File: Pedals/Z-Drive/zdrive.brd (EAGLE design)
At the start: 55.9 x 54.6 mm, 30 parts, among them IC1 MC1458P, Q1 2N7000, Q2 2N7000

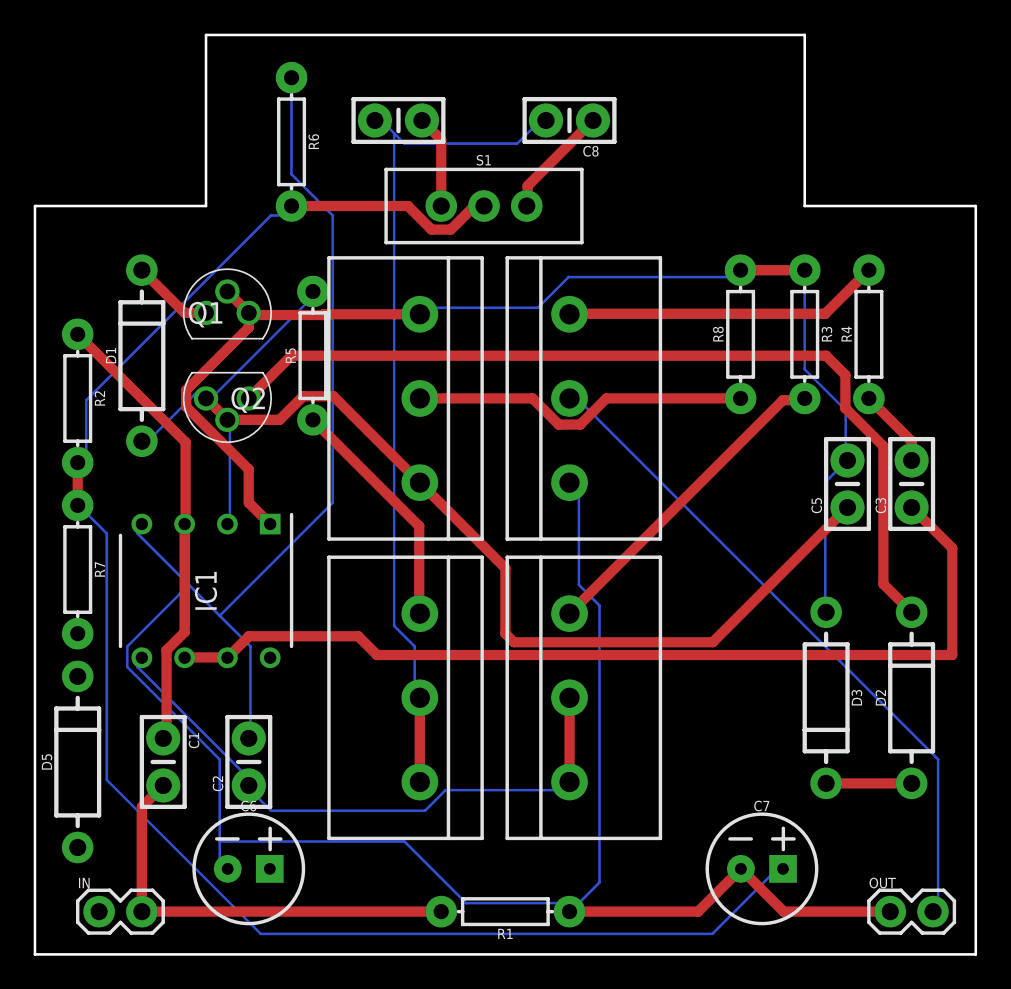
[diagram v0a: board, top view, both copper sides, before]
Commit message: Board routed V1
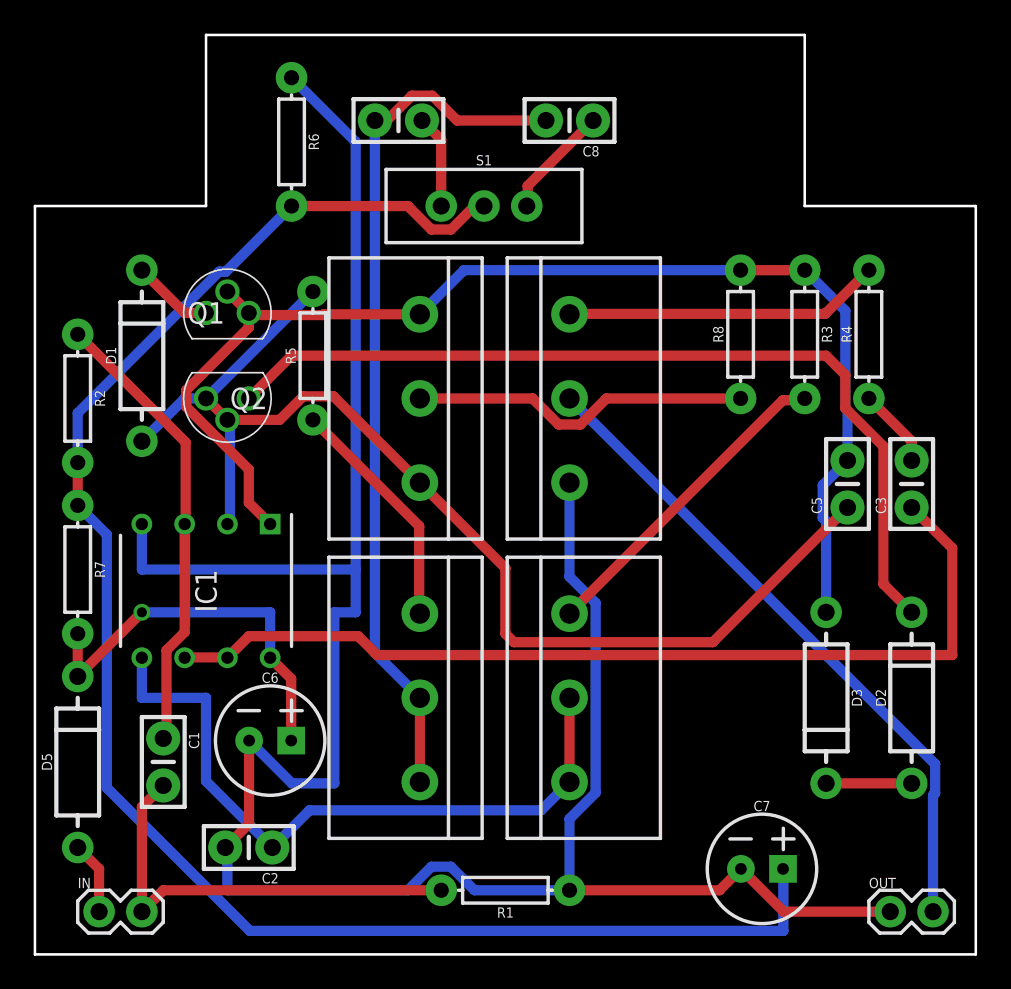
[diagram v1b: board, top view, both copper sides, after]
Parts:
- moved C6 7.73 mm to (14.0, 12.7)
- moved C2 5.08 mm to (12.7, 6.35), turned to 180 degrees
- moved R1 1.27 mm to (27.9, 3.81)
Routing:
- net V+: track 0.97 -> 23.7 mm, vias 0 -> 1
- net OP5: track 36.1 -> 41.0 mm
- net 9V: track 0.00 -> 4.34 mm
- net V2: track 99.1 -> 100.7 mm
- net N$7: track 50.6 -> 51.8 mm
- net OP2: track 71.8 -> 71.1 mm
- net IN: track 25.8 -> 26.3 mm

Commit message: Shift switch
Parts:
- moved S1 0.63 mm to (27.3, 44.5)
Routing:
- net V2: track 100.7 -> 101.4 mm
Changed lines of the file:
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@@
 <setting verticaltext="up"/>
 </settings>
-<grid distance="50" unitdist="mil" unit="mil" style="lines" multiple="1" display="yes" altdistance="5" altunitdist="mil" altunit="mil"/>
+<grid distance="25" unitdist="mil" unit="mil" style="lines" multiple="1" display="yes" altdistance="5" altunitdist="mil" altunit="mil"/>
 <layers>
 <layer number="1" name="Top" color="4" fill="1" visible="yes" active="yes"/>
@@
 </layers>
 <board>
-<fusionsync huburn="a.YnVzaW5lc3M6Z21haWwxNjcwNzYy" projecturn="a.YnVzaW5lc3M6Z21haWwxNjcwNzYyIzIwMjEwNDEyNDAyMDk1MzUx" f3durn="urn:adsk.wipprod:dm.lineage:s0TrARQBRNe1nJ0j_Cxp4Q" pcbguid="2e1078e5-0462-4d1c-b8a8-0c0597d6a6c0" lastpulledtime="" lastsyncedchangeguid="" latestrevisionid="c03cb7e0-1b01-40d5-a0a0-639d900d0ca0" lastsyncedrevisionid="c03cb7e0-1b01-40d5-a0a0-639d900d0ca0" lastboardhashguid="4b4d04b6-911f-26f5-6e83-cf409d0949b4" lastpushedtime="2021-04-13T14:10:19Z" linktopcb3d="true"/>
+<fusionsync huburn="a.YnVzaW5lc3M6Z21haWwxNjcwNzYy" projecturn="a.YnVzaW5lc3M6Z21haWwxNjcwNzYyIzIwMjEwNDEyNDAyMDk1MzUx" f3durn="urn:adsk.wipprod:dm.lineage:s0TrARQBRNe1nJ0j_Cxp4Q" pcbguid="" lastpulledtime="" lastsyncedchangeguid="" latestrevisionid="c03cb7e0-1b01-40d5-a0a0-639d900d0ca0" lastsyncedrevisionid="c03cb7e0-1b01-40d5-a0a0-639d900d0ca0" lastboardhashguid="4b4d04b6-911f-26f5-6e83-cf409d0949b4" lastpushedtime="2021-04-13T14:10:19Z" linktopcb3d="true"/>
 <plain>
 <wire x1="0" y1="44.45" x2="10.16" y2="44.45" width="0.1524" layer="20"/>
@@
 <attribute name="VALUE" x="42.926" y="36.83" size="0.6096" layer="27" font="vector" ratio="20" rot="R90" align="top-center"/>
 </element>
-<element name="S1" library="SparkFun-Switches" library_urn="urn:adsk.eagle:library:535" package="SWITCH_SPDT_PTH_11.6X4.0MM" package3d_urn="urn:adsk.eagle:package:40177/1" value="" x="26.67" y="44.45" smashed="yes" rot="R270">
-<attribute name="NAME" x="26.67" y="46.863" size="0.6096" layer="25" font="vector" ratio="20" align="bottom-center"/>
-<attribute name="PROD_ID" value="SWCH-08261" x="20.32" y="29.21" size="1.778" layer="27" rot="R270" display="off"/>
-<attribute name="SF_SKU" value="COM-00102" x="20.32" y="29.21" size="1.778" layer="27" rot="R270" display="off"/>
-<attribute name="VALUE" x="26.67" y="42.037" size="0.6096" layer="27" font="vector" ratio="20" align="top-center"/>
+<element name="S1" library="SparkFun-Switches" library_urn="urn:adsk.eagle:library:535" package="SWITCH_SPDT_PTH_11.6X4.0MM" package3d_urn="urn:adsk.eagle:package:40177/1" value="" x="27.305" y="44.45" smashed="yes" rot="R270">
+<attribute name="NAME" x="27.305" y="46.863" size="0.6096" layer="25" font="vector" ratio="20" align="bottom-center"/>
+<attribute name="PROD_ID" value="SWCH-08261" x="20.955" y="29.21" size="1.778" layer="27" rot="R270" display="off"/>
+<attribute name="SF_SKU" value="COM-00102" x="20.955" y="29.21" size="1.778" layer="27" rot="R270" display="off"/>
+<attribute name="VALUE" x="27.305" y="42.037" size="0.6096" layer="27" font="vector" ratio="20" align="top-center"/>
 </element>
 <element name="TONE" library="Custom-Parts" package="3RP/1610N" package3d_urn="urn:adsk.eagle:package:22726/1" value="B50k" x="31.75" y="15.24" smashed="yes" rot="R270">
@@
 <contactref element="R2" pad="P$2"/>
 <contactref element="S1" pad="2"/>
-<wire x1="23.5513375" y1="43.053" x2="24.7086625" y2="43.053" width="0.6096" layer="1"/>
 <wire x1="15.24" y1="44.45" x2="22.1543375" y2="44.45" width="0.6096" layer="1"/>
-<wire x1="26.1056625" y1="44.45" x2="26.67" y2="44.45" width="0.6096" layer="1"/>
 <wire x1="22.1543375" y1="44.45" x2="23.5513375" y2="43.053" width="0.6096" layer="1"/>
-<wire x1="24.7086625" y1="43.053" x2="26.1056625" y2="44.45" width="0.6096" layer="1"/>
 <wire x1="2.54" y1="29.21" x2="2.54" y2="26.67" width="0.6096" layer="1"/>
 <wire x1="4.2672" y1="9.89516875" x2="12.76536875" y2="1.397" width="0.6096" layer="16"/>
@@
 <wire x1="2.54" y1="26.67" x2="4.2672" y2="24.9428" width="0.6096" layer="16"/>
 <wire x1="4.2672" y1="24.9428" x2="4.2672" y2="9.89516875" width="0.6096" layer="16"/>
+<wire x1="25.908" y1="43.053" x2="27.305" y2="44.45" width="0.6096" layer="1"/>
+<wire x1="23.5513375" y1="43.053" x2="25.908" y2="43.053" width="0.6096" layer="1"/>
 </signal>
 <signal name="N$6">
@@
 <contactref element="S1" pad="3"/>
 <contactref element="C4" pad="1"/>
-<wire x1="22.987" y1="49.53" x2="24.13" y2="48.387" width="0.6096" layer="1"/>
-<wire x1="24.13" y1="48.387" x2="24.13" y2="44.45" width="0.6096" layer="1"/>
+<wire x1="22.987" y1="49.53" x2="24.765" y2="47.752" width="0.6096" layer="1"/>
+<wire x1="24.765" y1="47.752" x2="24.765" y2="44.45" width="0.6096" layer="1"/>
 </signal>
 <signal name="N$12">
 <contactref element="S1" pad="1"/>
 <contactref element="C8" pad="1"/>
-<wire x1="29.2608" y1="44.5008" x2="29.21" y2="44.45" width="0.1524" layer="1"/>
-<wire x1="33.147" y1="49.53" x2="29.2608" y2="45.6438" width="0.6096" layer="1"/>
-<wire x1="29.2608" y1="45.6438" x2="29.2608" y2="44.5008" width="0.6096" layer="1"/>
+<wire x1="33.147" y1="49.53" x2="33.147" y2="47.752" width="0.6096" layer="1"/>
+<wire x1="33.147" y1="47.752" x2="29.845" y2="44.45" width="0.6096" layer="1"/>
 </signal>
 </signals>

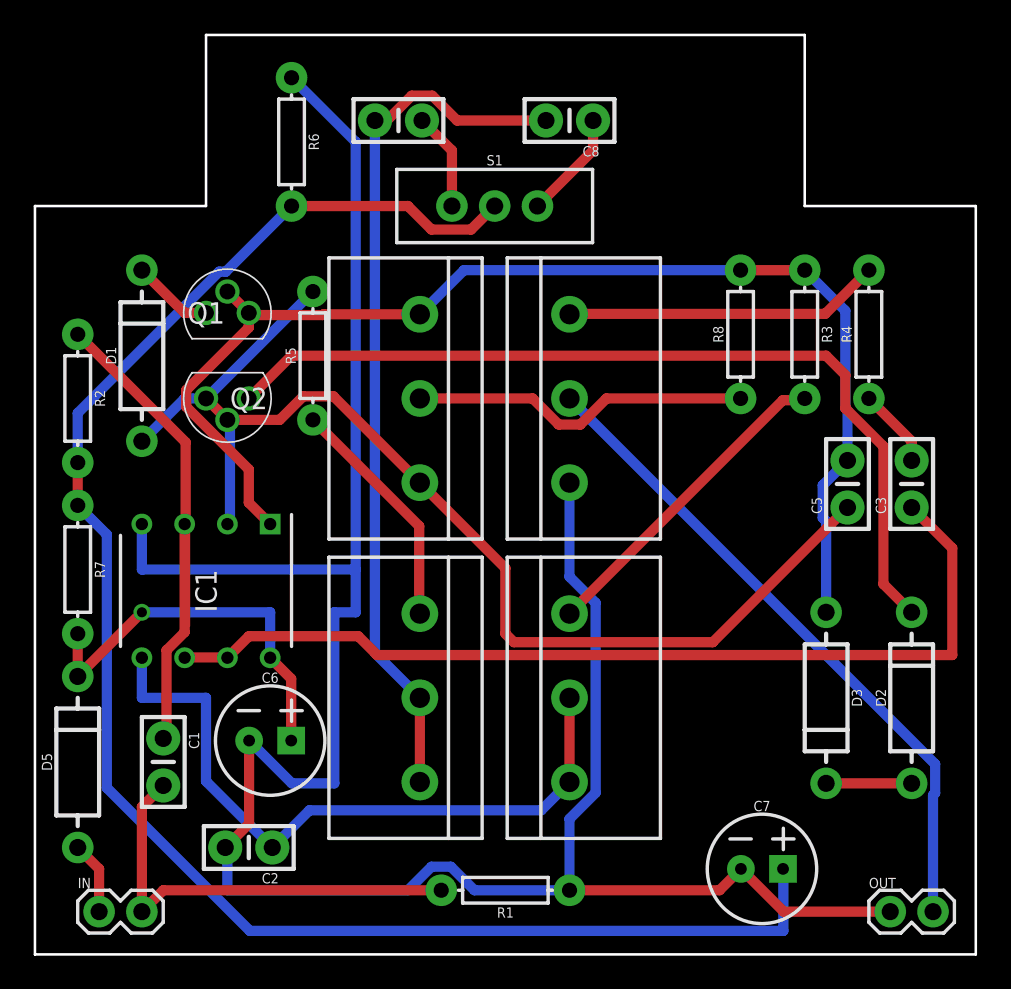
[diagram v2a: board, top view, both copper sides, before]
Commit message: Adjusted the pots
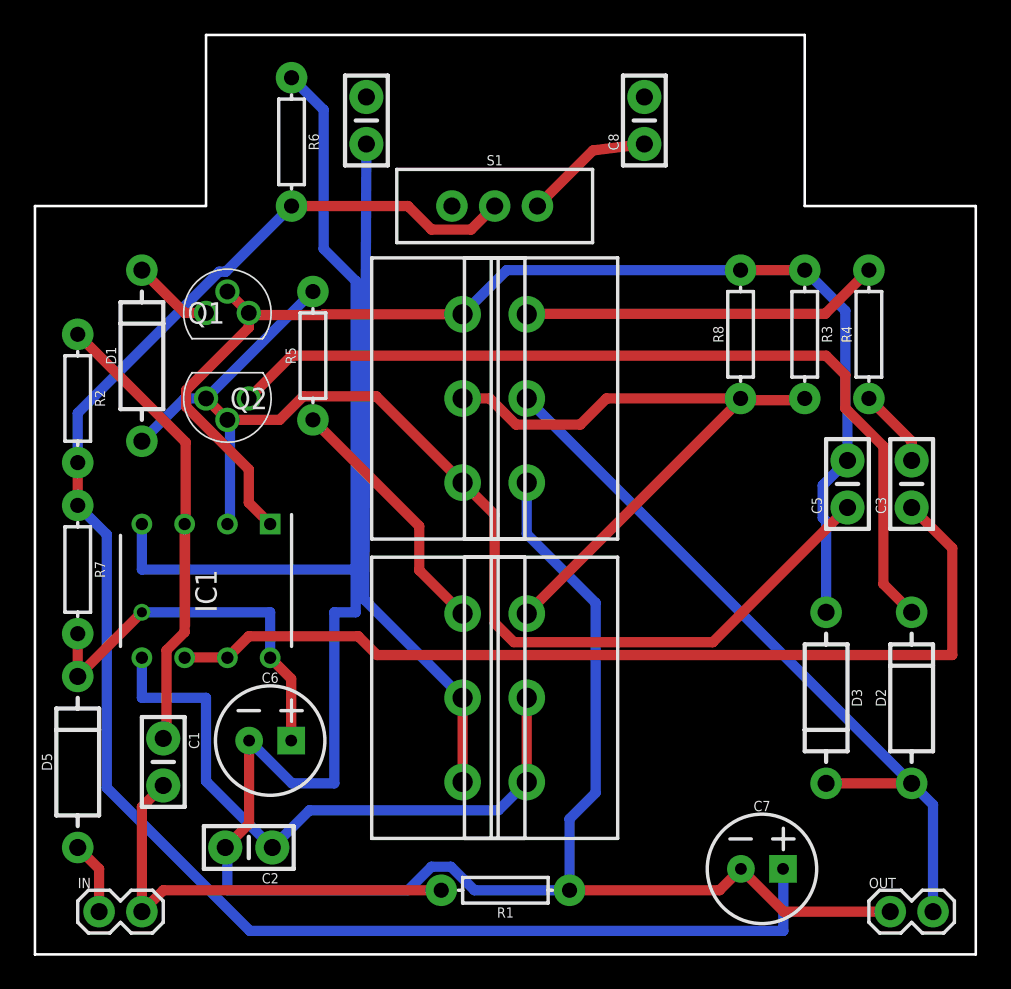
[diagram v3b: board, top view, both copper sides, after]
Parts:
- moved C8 4.45 mm to (36.2, 49.5), turned to 90 degrees
- moved GAIN 2.54 mm to (25.4, 33.0)
- moved TONE 2.54 mm to (29.2, 15.2)
- moved VOICE 2.54 mm to (25.4, 15.2)
- moved VOL 2.54 mm to (29.2, 33.0)
- moved C4 1.91 mm to (19.7, 49.5), turned to 270 degrees
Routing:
- net N$7: track 51.8 -> 40.3 mm
- net N$11: track 5.82 -> 0.00 mm
- net N$1: track 19.3 -> 21.9 mm
- net N$5: track 20.3 -> 17.8 mm
- net N$4: track 18.9 -> 21.4 mm
- net OP5: track 41.0 -> 38.4 mm
- net OP2: track 71.1 -> 72.5 mm
- net N$12: track 6.45 -> 7.74 mm
- net N$6: track 14.1 -> 15.2 mm
- net GND: track 143.4 -> 144.5 mm
- net OUT: track 39.5 -> 40.5 mm

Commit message: Rotate switch
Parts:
- moved C8 3.18 mm to (36.2, 46.4)
- moved S1 3.17 mm to (27.3, 47.6), turned to 180 degrees
- moved C4 1.42 mm to (21.0, 48.9)
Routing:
- net N$7: track 40.3 -> 56.6 mm
- net N$11: track 0.00 -> 6.40 mm
- net OUT: track 40.5 -> 46.4 mm
- net N$12: track 7.74 -> 8.94 mm

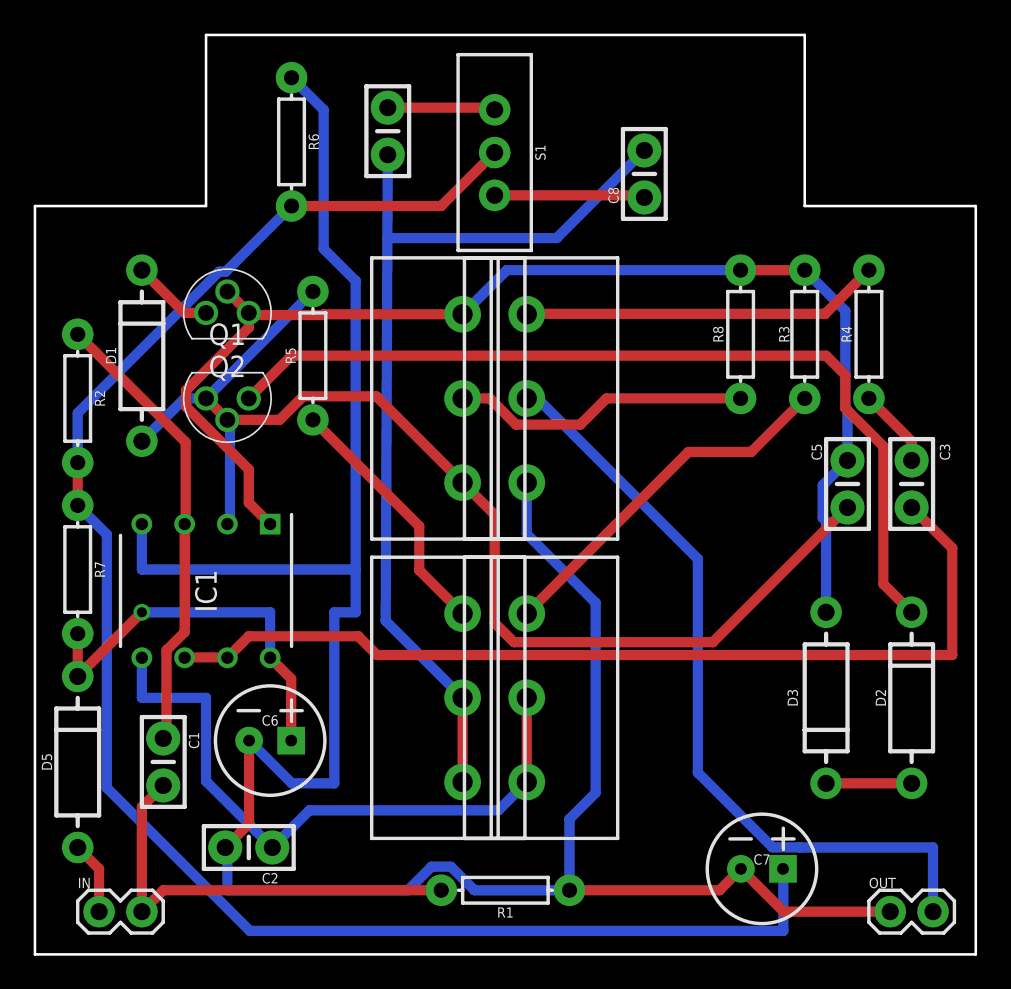
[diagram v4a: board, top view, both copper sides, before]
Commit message: Shift pots so they are centered
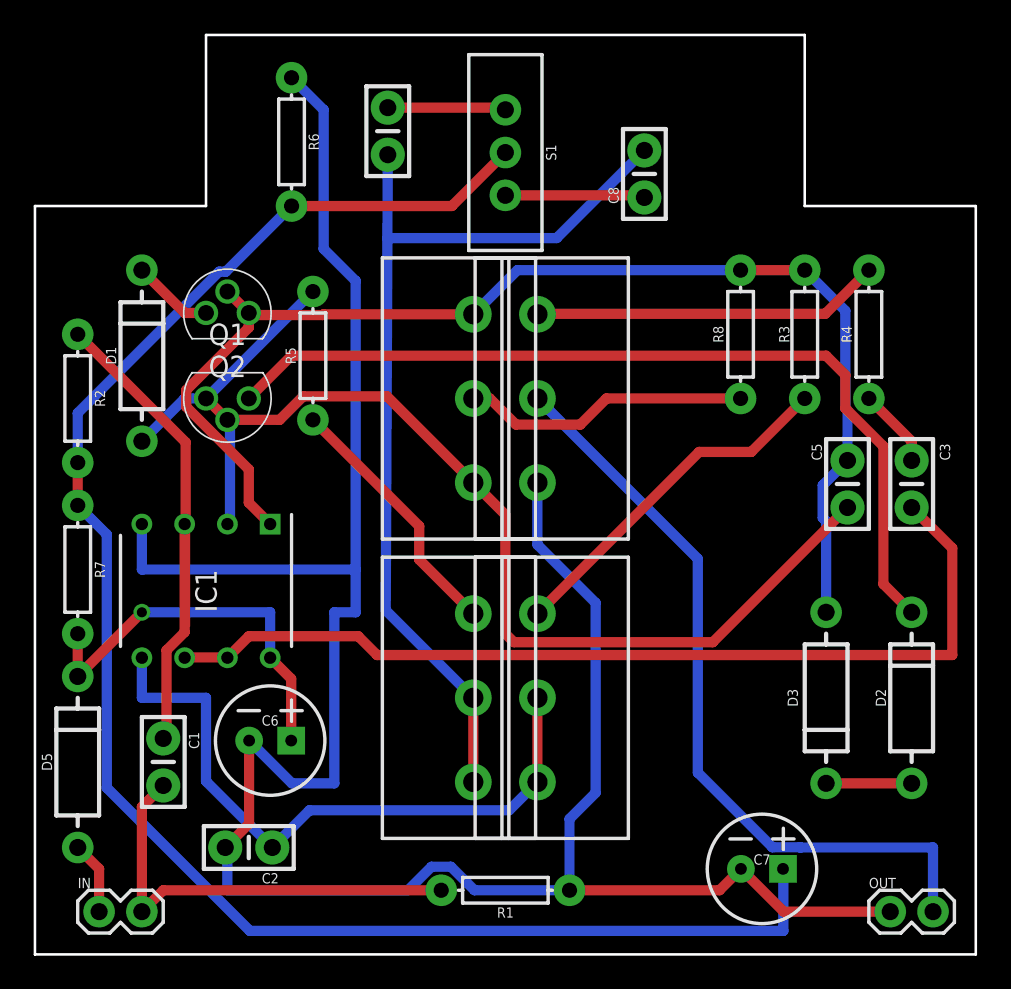
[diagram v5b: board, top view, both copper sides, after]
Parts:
- moved GAIN 0.64 mm to (26.0, 33.0)
- moved S1 0.64 mm to (27.9, 47.6)
- moved VOICE 0.64 mm to (26.0, 15.2)
- moved TONE 0.63 mm to (29.8, 15.2)
- moved VOL 0.63 mm to (29.8, 33.0)
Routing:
- net V2: track 101.5 -> 102.2 mm
- net N$5: track 17.8 -> 17.2 mm
- net N$12: track 8.94 -> 8.31 mm
- net N$1: track 21.8 -> 21.2 mm
- net N$11: track 6.40 -> 7.04 mm
- net OUT: track 46.4 -> 45.8 mm
- net N$4: track 21.4 -> 20.8 mm
- net OP5: track 38.4 -> 39.1 mm
